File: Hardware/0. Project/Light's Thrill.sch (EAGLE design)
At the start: 39 parts, among them CN1 Micro-USB, CN2 2.1MMJACKTHM, Q1 SI2302DS, Q2 SI2302DS, Q3 SI2302DS, U1 TSOP1838, U2 ATMEGA32U4, U3 LM1117-5.0, Y1 16 MHz

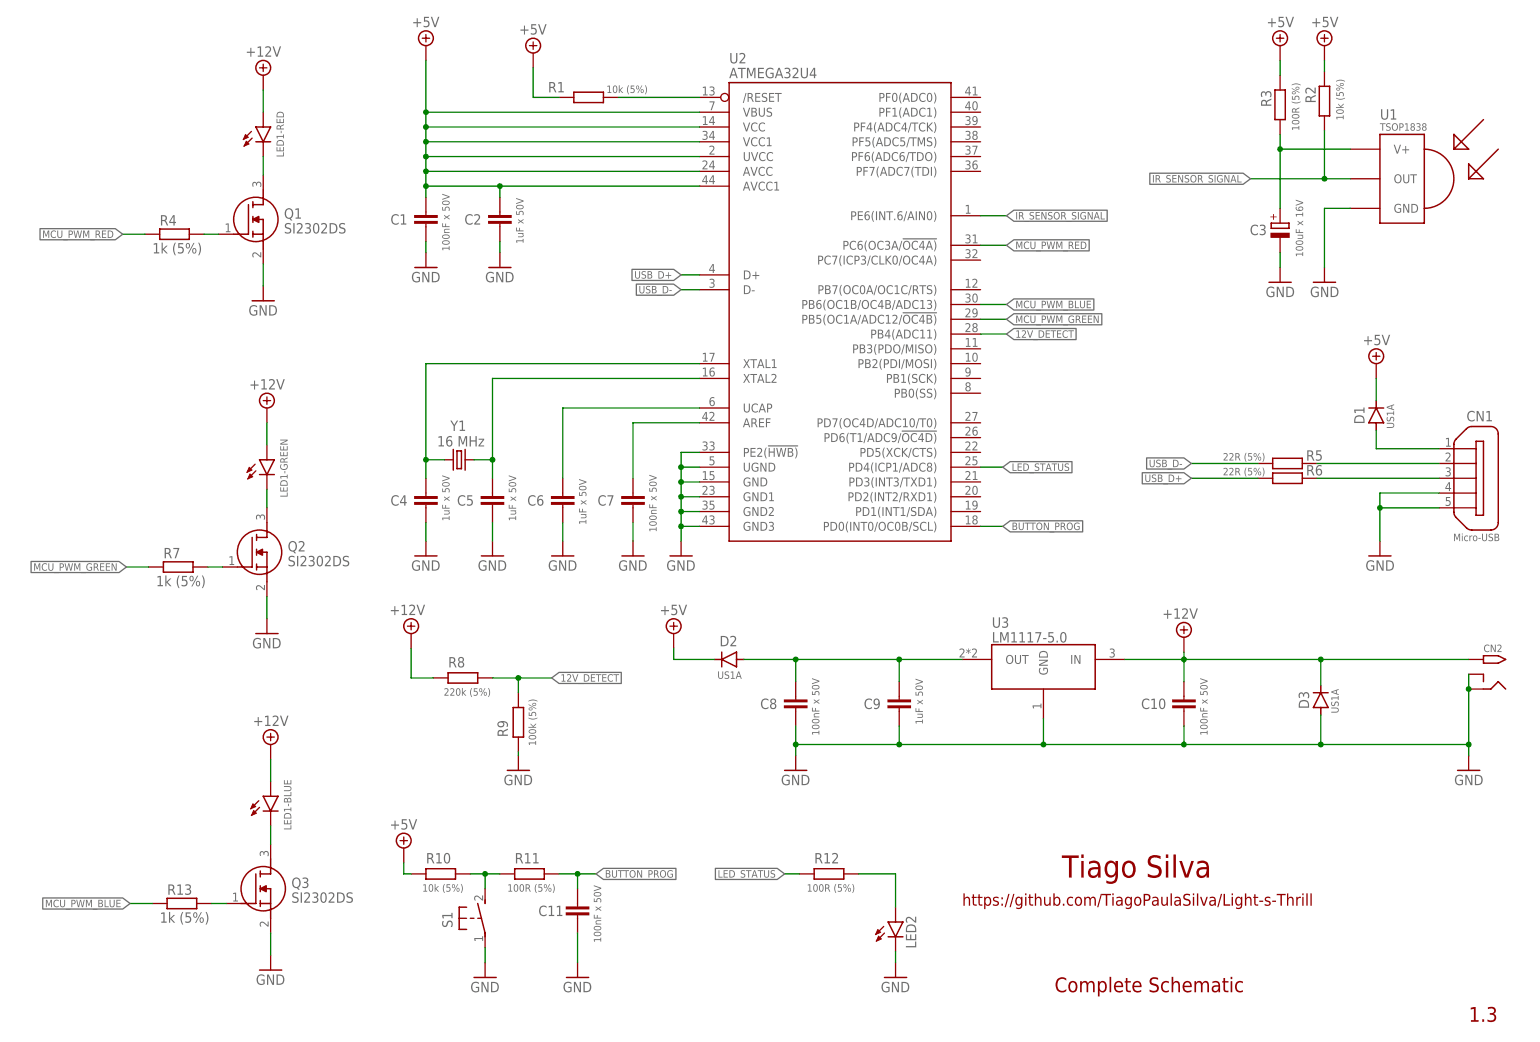
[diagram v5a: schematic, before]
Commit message: ICSP Programming added (PCB 1.4)
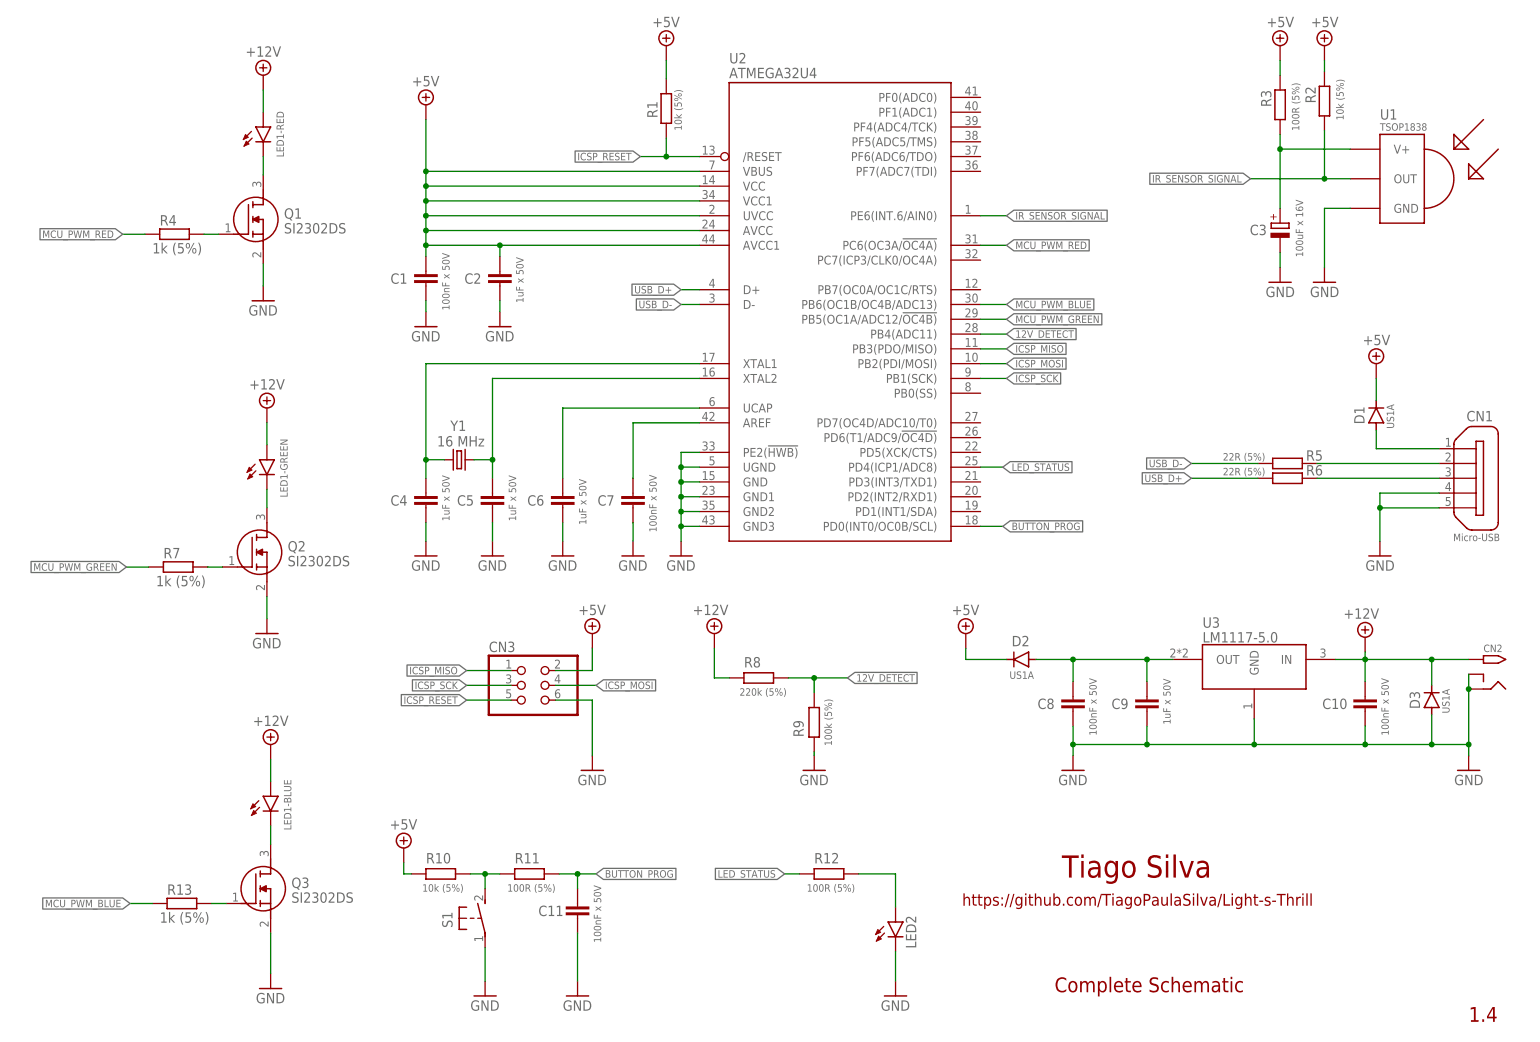
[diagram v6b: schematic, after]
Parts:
- added CN3: 2x3, pinhead:PINHD-2X3
- LED2: value (none) -> Red
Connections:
- removed net N$10: R1.1, U2./RESET
- new net ICSP_MISO: CN3.1, U2.PB3(PDO/MISO)
- new net ICSP_MOSI: CN3.4, U2.PB2(PDI/MOSI)
- new net ICSP_RESET: CN3.5, R1.1, U2./RESET
- new net ICSP_SCK: CN3.3, U2.PB1(SCK)
- net +5V: now also CN3.2
- net GND: now also CN3.6
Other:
- note added: "1.4"
- note added: "D8"
- note removed: "1.3"
- note removed: "D2"
- moved on the sheet: C1, C10, C2, C8, C9, D2, D3, R1, R8, R9, U3
